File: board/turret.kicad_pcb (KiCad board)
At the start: 2 copper layers, 28 parts, among them Q1 2N3904, U1 W25Q32JVSS, U2 LM386

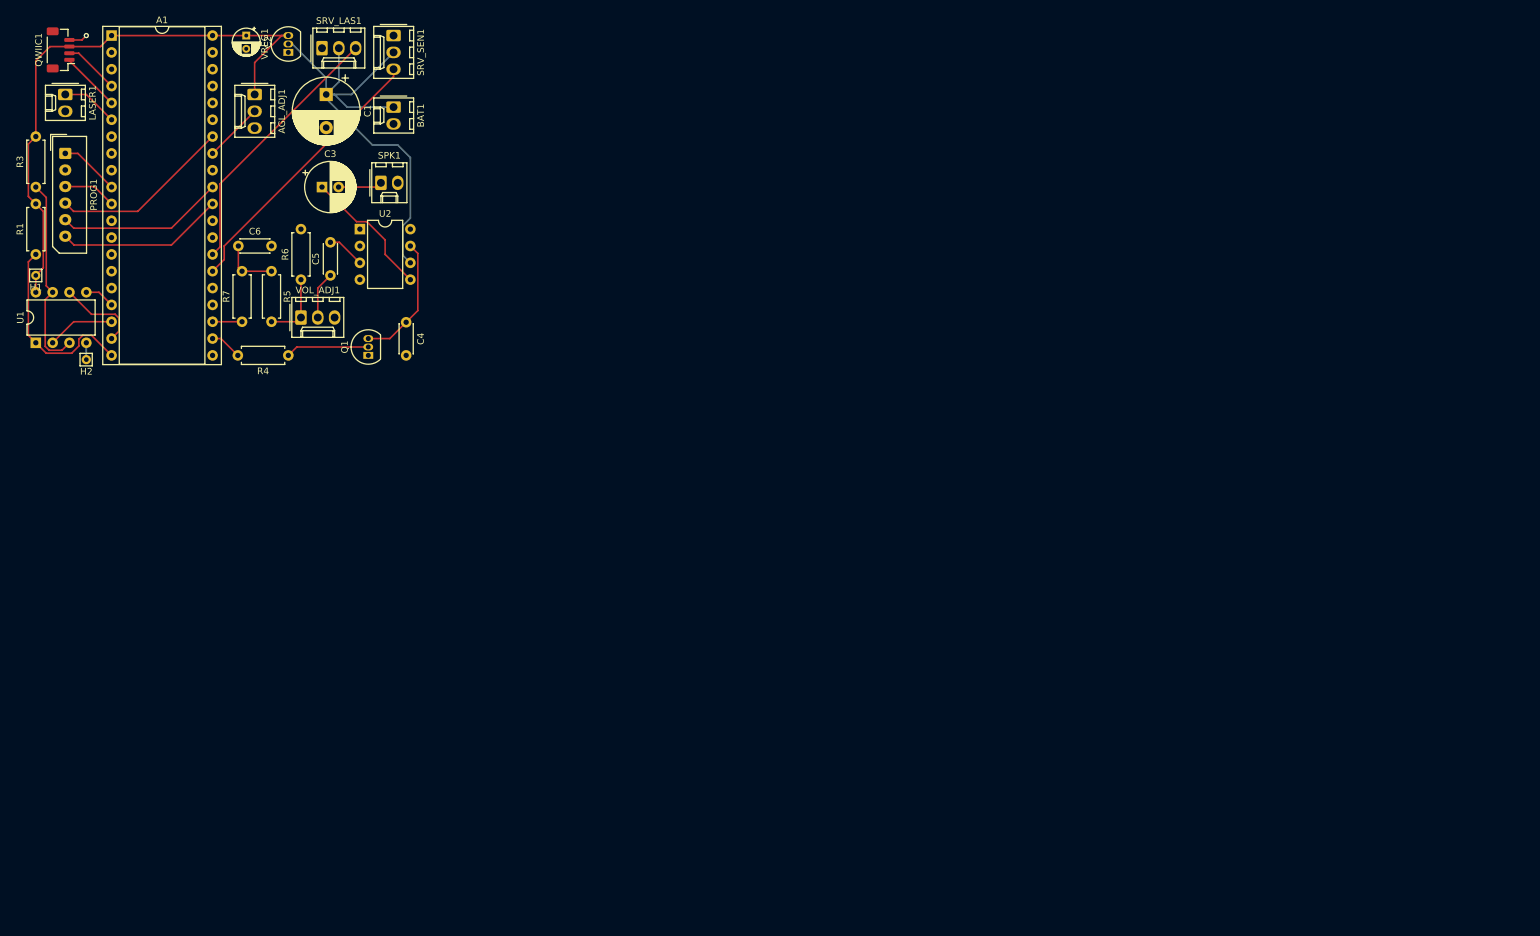
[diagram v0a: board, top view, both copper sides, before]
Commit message: Assign most components
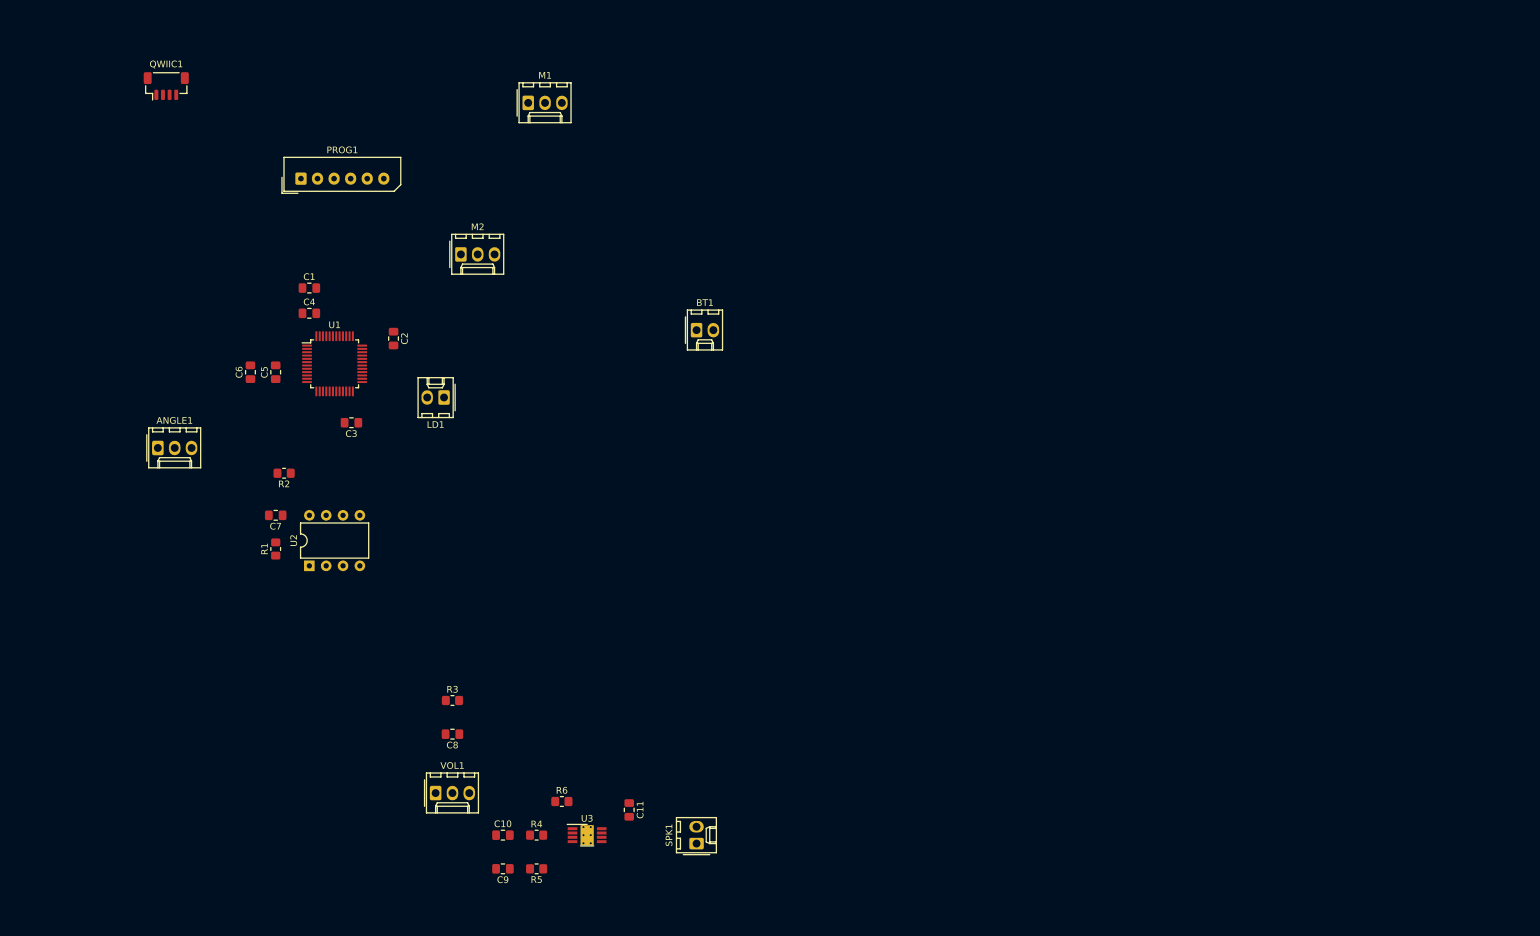
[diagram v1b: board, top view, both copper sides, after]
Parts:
- removed A1: Maple_Mini, Package_DIP:DIP-40_W15.24mm_Socket
- removed AGL_ADJ1: 10K, Connector_Molex:Molex_KK-254_AE-6410-03A_1x03_P2.54mm_Vertical
- removed BAT1: Battery, Connector_Molex:Molex_KK-254_AE-6410-02A_1x02_P2.54mm_Vertical
- removed H1: CAP_POS, Connector_Pin:Pin_D0.7mm_L6.5mm_W1.8mm_FlatFork
- removed H2: CAP_NEG, Connector_Pin:Pin_D0.7mm_L6.5mm_W1.8mm_FlatFork
- removed LASER1: Conn_01x02, Connector_Molex:Molex_KK-254_AE-6410-02A_1x02_P2.54mm_Vertical
- removed Q1: 2N3904, Package_TO_SOT_THT:TO-92_Inline
- removed R7: 560, Resistor_THT:R_Axial_DIN0207_L6.3mm_D2.5mm_P7.62mm_Horizontal
- removed SRV_LAS1, SRV_SEN1: Conn_01x03, Connector_Molex:Molex_KK-254_AE-6410-03A_1x03_P2.54mm_Vertical
- removed VOL_ADJ1: 2K, Connector_Molex:Molex_KK-254_AE-6410-03A_1x03_P2.54mm_Vertical
- removed VREG1: MCP1700-3302E_TO92, Package_TO_SOT_THT:TO-92_Inline
- added ANGLE1: 10K, Connector_Molex:Molex_KK-254_AE-6410-03A_1x03_P2.54mm_Vertical, F.Cu at (39.4, 77.5)
- added BT1: Battery, Connector_Molex:Molex_KK-254_AE-6410-02A_1x02_P2.54mm_Vertical, F.Cu at (120.7, 59.7)
- added C10: 10n, Capacitor_SMD:C_0805_2012Metric_Pad1.18x1.45mm_HandSolder, F.Cu at (91.4, 135.9)
- added C11: 100n, Capacitor_SMD:C_0805_2012Metric_Pad1.18x1.45mm_HandSolder, F.Cu at (110.5, 132.1)
- added C7: 100n, Capacitor_SMD:C_0805_2012Metric_Pad1.18x1.45mm_HandSolder, F.Cu at (57.1, 87.6)
- added C8: 100n, Capacitor_SMD:C_0805_2012Metric_Pad1.18x1.45mm_HandSolder, F.Cu at (83.8, 120.7)
- added C9: 10n, Capacitor_SMD:C_0805_2012Metric_Pad1.18x1.45mm_HandSolder, F.Cu at (91.4, 141.0)
- added LD1: Laserdiode_1C2A, Connector_Molex:Molex_KK-254_AE-6410-02A_1x02_P2.54mm_Vertical, F.Cu at (82.5, 69.8)
- added M1: SRV_LAS, Connector_Molex:Molex_KK-254_AE-6410-03A_1x03_P2.54mm_Vertical, F.Cu at (95.2, 25.4)
- added M2: SRV_SEN, Connector_Molex:Molex_KK-254_AE-6410-03A_1x03_P2.54mm_Vertical, F.Cu at (85.1, 48.3)
- added R2: 50K, Resistor_SMD:R_0805_2012Metric_Pad1.20x1.40mm_HandSolder, F.Cu at (58.4, 81.3)
- added U3: TPA2005D1DGN, Custom_IC:TI_VSSOP-PowerPAD-8_3.0x3.0mm_P0.65mm_ThermalVias, F.Cu at (104.1, 135.9)
- added VOL1: 10K, Connector_Molex:Molex_KK-254_AE-6410-03A_1x03_P2.54mm_Vertical, F.Cu at (81.3, 129.5)
- C1: value 1000uF -> 4u7; footprint Capacitor_THT:CP_Radial_D10.0mm_P5.00mm -> Capacitor_SMD:C_0805_2012Metric_Pad1.18x1.45mm_HandSolder
- C2: value 1uF -> 100n; footprint Capacitor_THT:CP_Radial_D4.0mm_P2.00mm -> Capacitor_SMD:C_0805_2012Metric_Pad1.18x1.45mm_HandSolder
- C3: value 220uF -> 100n; footprint Capacitor_THT:CP_Radial_D7.5mm_P2.50mm -> Capacitor_SMD:C_0805_2012Metric_Pad1.18x1.45mm_HandSolder
- C4: value 100 nF -> 100n; footprint Capacitor_THT:C_Disc_D4.3mm_W1.9mm_P5.00mm -> Capacitor_SMD:C_0805_2012Metric_Pad1.18x1.45mm_HandSolder
- C5: value 100 nF -> 1u; footprint Capacitor_THT:C_Disc_D4.3mm_W1.9mm_P5.00mm -> Capacitor_SMD:C_0805_2012Metric_Pad1.18x1.45mm_HandSolder
- C6: value 10 nF -> 10n; footprint Capacitor_THT:C_Disc_D4.3mm_W1.9mm_P5.00mm -> Capacitor_SMD:C_0805_2012Metric_Pad1.18x1.45mm_HandSolder
- R1: value 10K -> 50K; footprint Resistor_THT:R_Axial_DIN0207_L6.3mm_D2.5mm_P7.62mm_Horizontal -> Resistor_SMD:R_0805_2012Metric_Pad1.20x1.40mm_HandSolder
- R3: value 10K -> 400; footprint Resistor_THT:R_Axial_DIN0207_L6.3mm_D2.5mm_P7.62mm_Horizontal -> Resistor_SMD:R_0805_2012Metric_Pad1.20x1.40mm_HandSolder
- R4: value 1000K -> 150K; footprint Resistor_THT:R_Axial_DIN0207_L6.3mm_D2.5mm_P7.62mm_Horizontal -> Resistor_SMD:R_0805_2012Metric_Pad1.20x1.40mm_HandSolder
- R5: value 10K -> 150K; footprint Resistor_THT:R_Axial_DIN0207_L6.3mm_D2.5mm_P7.62mm_Horizontal -> Resistor_SMD:R_0805_2012Metric_Pad1.20x1.40mm_HandSolder
- R6: value 1K -> 50K; footprint Resistor_THT:R_Axial_DIN0207_L6.3mm_D2.5mm_P7.62mm_Horizontal -> Resistor_SMD:R_0805_2012Metric_Pad1.20x1.40mm_HandSolder
- SPK1: value Conn_01x02 -> Speaker
- U1: value W25Q32JVSS -> STM32F103CBTx; footprint Package_DIP:DIP-8_W7.62mm -> Package_QFP:LQFP-48_7x7mm_P0.5mm
- U2: value LM386 -> W25Q32JVSS
- moved SPK1 110.5 mm to (120.7, 137.2), turned to 90 degrees
- moved R3 99.8 mm to (83.8, 115.6), turned to 0 degrees
- moved R5 98.6 mm to (96.5, 141.0), turned to 180 degrees
- moved R6 88.0 mm to (100.3, 130.8), turned to 0 degrees
- moved R4 81.5 mm to (96.5, 135.9), turned to 0 degrees
- moved R1 57.3 mm to (57.1, 92.7)
- moved U2 51.4 mm to (62.2, 95.2), turned to 90 degrees
- moved C2 50.8 mm to (74.9, 61.0)
- moved U1 45.2 mm to (66.0, 64.8), turned to 0 degrees
- moved C3 35.8 mm to (68.6, 73.7), turned to 180 degrees
- moved PROG1 35.8 mm to (61.0, 36.8), turned to 0 degrees
- moved C1 29.3 mm to (62.2, 53.3), turned to 0 degrees
- moved C6 19.1 mm to (53.3, 66.0), turned to 90 degrees
- moved QWIIC1 16.9 mm to (40.6, 22.9), turned to 0 degrees
- moved C5 16.8 mm to (57.1, 66.0)
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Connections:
- C1 pad 1: +6V -> +3V3
- C1 pad 2: GND -> GNDA
- C2 pad 2: GND -> GNDA
- C3 pad 1: Net-(C3-Pad1) -> +3V3
- C3 pad 2: Net-(C3-Pad2) -> GNDA
- C4 pad 1: Net-(C4-Pad1) -> +3V3
- C4 pad 2: GND -> GNDA
- C5 pad 1: Net-(C5-Pad1) -> +3V3
- C5 pad 2: Net-(C5-Pad2) -> GNDA
- C6 pad 1: Net-(C6-Pad1) -> +3V3
- C6 pad 2: GND -> GNDA
- PROG1 pad 1: Net-(A1-Pad10) -> /SWCLK
- PROG1 pad 2: GND -> GNDA
- PROG1 pad 3: Net-(A1-Pad11) -> /SWDIO
- PROG1 pad 4: Net-(A1-Pad34) -> /RESET
- PROG1 pad 5: Net-(A1-Pad31) -> /SER_TX
- PROG1 pad 6: Net-(A1-Pad30) -> /SER_RX
- QWIIC1 pad 1: Net-(A1-Pad5) -> GNDA
- QWIIC1 pad 2: Net-(A1-Pad4) -> +3V3
- QWIIC1 pad 3: +3V3 -> /SDA
- QWIIC1 pad 4: GND -> /SCL
- R1 pad 1: Net-(A1-Pad20) -> /SPI_NSS
- R3 pad 1: Net-(R3-Pad1) -> /AUDIO
- R3 pad 2: +3V3 -> Net-(C8-Pad1)
- R4 pad 2: Mute -> Net-(R4-Pad2)
- R5 pad 1: Net-(C6-Pad1) -> Net-(R5-Pad1)
- R5 pad 2: Net-(R5-Pad2) -> Net-(C9-Pad1)
- R6 pad 1: Net-(R5-Pad2) -> /MUTE
- R6 pad 2: GND -> Net-(R6-Pad2)
- SPK1 pad 1: Net-(C3-Pad2) -> Net-(SPK1-Pad1)
- SPK1 pad 2: GND -> Net-(SPK1-Pad2)
- U1 pad 1: Net-(A1-Pad20) -> +3V3
- U1 pad 2: Net-(A1-Pad18) -> (no net)
- U1 pad 3: Net-(R3-Pad1) -> (no net)
- U1 pad 4: GND -> (no net)
- U1 pad 5: Net-(A1-Pad17) -> (no net)
- U1 pad 6: Net-(A1-Pad19) -> (no net)
- U1 pad 7: Net-(R3-Pad1) -> /RESET
- U1 pad 8: +3V3 -> GNDA
- U2 pad 1: Net-(U2-Pad1) -> /SPI_NSS
- U2 pad 2: GND -> /SPI_MISO
- U2 pad 3: Net-(C5-Pad2) -> Net-(R2-Pad1)
- U2 pad 4: GND -> GNDA
- U2 pad 5: Net-(C3-Pad1) -> /SPI_MOSI
- U2 pad 6: +6V -> /SPI_SCK
- U2 pad 7: Net-(C4-Pad1) -> Net-(R2-Pad1)
- U2 pad 8: Net-(U2-Pad8) -> +3V3
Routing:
- net +3V3: track 88.0 -> 0.00 mm
- net +6V: track 75.7 -> 0.00 mm
- net SRV_SEN: track 41.8 -> 0.00 mm
- net SRV_LAS: track 40.1 -> 0.00 mm
- net Net-(R3-Pad1): track 29.9 -> 0.00 mm
- net Net-(A1-Pad20): track 29.3 -> 0.00 mm
- net Net-(A1-Pad34): track 27.4 -> 0.00 mm
- net Net-(A1-Pad30): track 25.3 -> 0.00 mm
- net Net-(A1-Pad31): track 25.3 -> 0.00 mm
- net Net-(C3-Pad1): track 20.4 -> 0.00 mm
- net Net-(C4-Pad1): track 19.4 -> 0.00 mm
- net Net-(A1-Pad19): track 12.6 -> 0.00 mm
- net Net-(C10-Pad2): track 12.6 -> 0.00 mm
- net Net-(R5-Pad2): track 10.4 -> 0.00 mm
- net Net-(A1-Pad18): track 10.2 -> 0.00 mm
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
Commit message: Add PCB design
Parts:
- added C12: 22u, Capacitor_SMD:C_0603_1608Metric, F.Cu at (92.6, 67.3)
- added C13: 22u, Capacitor_SMD:C_0603_1608Metric, F.Cu at (92.6, 65.4)
- added C14: 4u7, Capacitor_SMD:C_0603_1608Metric, F.Cu at (91.4, 62.7)
- added C15: 100n, Capacitor_SMD:C_0603_1608Metric, F.Cu at (79.5, 52.1)
- added C16: 100n, Capacitor_SMD:C_0603_1608Metric, F.Cu at (79.5, 58.4)
- added C17: 1000u, Capacitor_THT:CP_Radial_D10.0mm_P5.00mm, F.Cu at (91.4, 56.5)
- added C18: 100p, Capacitor_SMD:C_0603_1608Metric, F.Cu at (91.9, 77.5)
- added C19: 20p, Capacitor_SMD:C_0603_1608Metric, F.Cu at (91.9, 79.4)
- added D1: LED, LED_SMD:LED_0805_2012Metric, F.Cu at (70.5, 56.6)
- added D2: D_Schottky, Diode_SMD:D_SMA, F.Cu at (90.1, 74.9)
- added L1: 2u2, Inductor_THT:L_Axial_L7.0mm_D3.3mm_P10.16mm_Horizontal_Fastron_MICC, F.Cu at (88.3, 71.8)
- added Q1: BC547, Package_TO_SOT_THT:TO-92_Inline_Wide, F.Cu at (97.2, 82.5)
- added R7: 5, Resistor_SMD:R_0603_1608Metric, F.Cu at (88.5, 77.5)
- added R8: 1K, Resistor_SMD:R_0603_1608Metric, F.Cu at (87.4, 82.5)
- added U4: TPS61322xADBV, Package_TO_SOT_SMD:SOT-23-5, F.Cu at (92.7, 70.5)
- added U5: TLV70028_SOT23-5, Package_TO_SOT_SMD:SOT-23-5, F.Cu at (79.4, 55.2)
- C1, C10, C11, C2, C3, C4, C5, C6, C8, C9: footprint Capacitor_SMD:C_0805_2012Metric_Pad1.18x1.45mm_HandSolder -> Capacitor_SMD:C_0603_1608Metric
- C7: footprint Capacitor_SMD:C_0805_2012Metric_Pad1.18x1.45mm_HandSolder -> Capacitor_SMD:C_0603_1608Metric; moved to B.Cu
- R1, R4, R5: footprint Resistor_SMD:R_0805_2012Metric_Pad1.20x1.40mm_HandSolder -> Resistor_SMD:R_0603_1608Metric
- R2: footprint Resistor_SMD:R_0805_2012Metric_Pad1.20x1.40mm_HandSolder -> Resistor_SMD:R_0603_1608Metric; moved to B.Cu
- R3: value 400 -> 200; footprint Resistor_SMD:R_0805_2012Metric_Pad1.20x1.40mm_HandSolder -> Resistor_SMD:R_0603_1608Metric
- R6: value 50K -> 50; footprint Resistor_SMD:R_0805_2012Metric_Pad1.20x1.40mm_HandSolder -> Resistor_SMD:R_0603_1608Metric
- moved R6 78.3 mm to (70.5, 58.4), turned to 180 degrees
- moved SPK1 68.3 mm to (78.7, 83.2)
- moved R5 66.0 mm to (64.6, 83.2)
- moved C9 65.1 mm to (61.4, 83.2)
- moved U3 63.9 mm to (69.8, 81.9)
- moved R4 63.8 mm to (64.6, 80.6)
- moved C10 62.9 mm to (61.4, 80.6)
- moved C11 62.0 mm to (74.3, 81.8)
- moved VOL1 55.9 mm to (52.1, 81.9)
- moved C8 51.1 mm to (65.4, 73.0), turned to 0 degrees
- moved R3 48.1 mm to (65.4, 71.1), turned to 180 degrees
- moved M1 47.5 mm to (102.2, 72.4), turned to 90 degrees
- moved QWIIC1 35.4 mm to (61.6, 51.4)
- moved C7 30.1 mm to (74.9, 63.4), turned to 90 degrees
- moved R1 26.1 mm to (71.1, 70.6), turned to 270 degrees
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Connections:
- ANGLE1 pad 3: +3V3 -> VDD
- BT1 pad 1: +3V3 -> Net-(BT1-Pad1)
- BT1 pad 2: (no net) -> GNDA
- C1 pad 1: +3V3 -> VDD
- C11 pad 2: +3V3 -> +5V
- C2 pad 1: +3V3 -> VDD
- C3 pad 1: +3V3 -> VDD
- C4 pad 1: +3V3 -> VDD
- C5 pad 1: +3V3 -> VDD
- C6 pad 1: +3V3 -> VDD
- C7 pad 1: +3V3 -> VDD
- LD1 pad 1: GNDA -> Net-(LD1-Pad1)
- LD1 pad 2: /LASER -> +5V
- M1 pad 2: +3V3 -> +5V
- M2 pad 2: +3V3 -> +5V
- QWIIC1 pad 2: +3V3 -> VDD
- R1 pad 2: +3V3 -> VDD
- R2 pad 2: +3V3 -> VDD
- R6 pad 1: /MUTE -> Net-(D1-Pad2)
- R6 pad 2: Net-(R6-Pad2) -> /TGT_LED
- U1 pad 1: +3V3 -> VDD
- U1 pad 10: (no net) -> Net-(U1-Pad10)
- U1 pad 14: /SPI_NSS -> /AU_ENAB
- U1 pad 15: /SPI_SCK -> /LASER
- U1 pad 16: /SPI_MISO -> Net-(U1-Pad16)
- U1 pad 17: /SPI_MOSI -> Net-(U1-Pad17)
- U1 pad 18: (no net) -> /AUDIO
- U1 pad 19: (no net) -> Net-(U1-Pad19)
- U1 pad 2: (no net) -> Net-(U1-Pad2)
- U1 pad 20: (no net) -> Net-(U1-Pad20)
- U1 pad 21: (no net) -> Net-(U1-Pad21)
- U1 pad 22: (no net) -> Net-(U1-Pad22)
- U1 pad 24: +3V3 -> VDD
- U1 pad 25: (no net) -> /SPI_NSS
- U1 pad 26: (no net) -> /SPI_SCK
- U1 pad 27: /LASER -> /SPI_MISO
- U1 pad 28: (no net) -> /SPI_MOSI
- U1 pad 29: /AUDIO -> /SRV_SEN
- U1 pad 3: (no net) -> Net-(U1-Pad3)
- U1 pad 30: /MUTE -> /SRV_LAS
- U1 pad 31: (no net) -> Net-(U1-Pad31)
- U1 pad 32: (no net) -> Net-(U1-Pad32)
- U1 pad 33: (no net) -> Net-(U1-Pad33)
- U1 pad 36: +3V3 -> VDD
- U1 pad 38: (no net) -> Net-(U1-Pad38)
- U1 pad 39: (no net) -> /TGT_LED
- U1 pad 4: (no net) -> Net-(U1-Pad4)
- U1 pad 40: /SRV_SEN -> Net-(U1-Pad40)
- U1 pad 41: /SRV_LAS -> Net-(U1-Pad41)
- U1 pad 44: (no net) -> Net-(U1-Pad44)
- U1 pad 45: (no net) -> Net-(U1-Pad45)
- U1 pad 46: (no net) -> Net-(U1-Pad46)
- U1 pad 48: +3V3 -> VDD
- U1 pad 5: (no net) -> Net-(U1-Pad5)
- U1 pad 6: (no net) -> Net-(U1-Pad6)
- U1 pad 9: +3V3 -> VDD
- U2 pad 8: +3V3 -> VDD
- U3 pad 1: Net-(R6-Pad2) -> /AU_ENAB
- U3 pad 2: (no net) -> Net-(U3-Pad2)
- U3 pad 6: +3V3 -> +5V
- U3 pad 9: (no net) -> GNDA
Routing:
- net GNDA: track 0.00 -> 103.0 mm, vias 0 -> 14
- net VDD: track 0.00 -> 89.2 mm, vias 0 -> 2
- net +5V: track 0.00 -> 78.8 mm, vias 0 -> 2
- net /SRV_LAS: track 0.00 -> 69.0 mm
- net /SRV_SEN: track 0.00 -> 58.6 mm
- net Net-(BT1-Pad1): track 0.00 -> 42.3 mm, vias 0 -> 3
- net /LASER: track 0.00 -> 32.6 mm
- net /SPI_SCK: track 0.00 -> 24.9 mm
- net /SWCLK: track 0.00 -> 23.4 mm, vias 0 -> 1
- net /SWDIO: track 0.00 -> 20.9 mm, vias 0 -> 1
- net Net-(C8-Pad1): track 0.00 -> 15.9 mm, vias 0 -> 2
- net /RESET: track 0.00 -> 15.5 mm, vias 0 -> 1
- net /SER_TX: track 0.00 -> 14.4 mm, vias 0 -> 1
- net /AU_ENAB: track 0.00 -> 14.2 mm
- net /SER_RX: track 0.00 -> 13.8 mm, vias 0 -> 1
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- added copper zone on B.Cu, net GNDA
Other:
- board outline added: 57.1 x 38.7 mm
- net class PWR added: clearance 0.2, trace_width 0.4, via_dia 0.8, via_drill 0.4

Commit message: Reroute 3v3 power
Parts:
- moved R1 2.62 mm to (71.8, 73.2), turned to 90 degrees
- moved C5 1.91 mm to (57.8, 65.9)
- moved C6 1.91 mm to (59.7, 65.9)
- moved R2 0.80 mm to (78.1, 63.5), turned to 90 degrees
- moved C7 0.12 mm to (74.9, 63.5)
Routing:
- net /SER_TX: track 14.4 -> 30.2 mm, vias 1 -> 0
- net /SER_RX: track 13.8 -> 27.9 mm, vias 1 -> 0
- net /SPI_NSS: track 8.73 -> 12.4 mm
- net /RESET: track 15.5 -> 12.3 mm, vias 1 -> 0
- net VDD: track 89.2 -> 92.2 mm, vias 2 -> 5

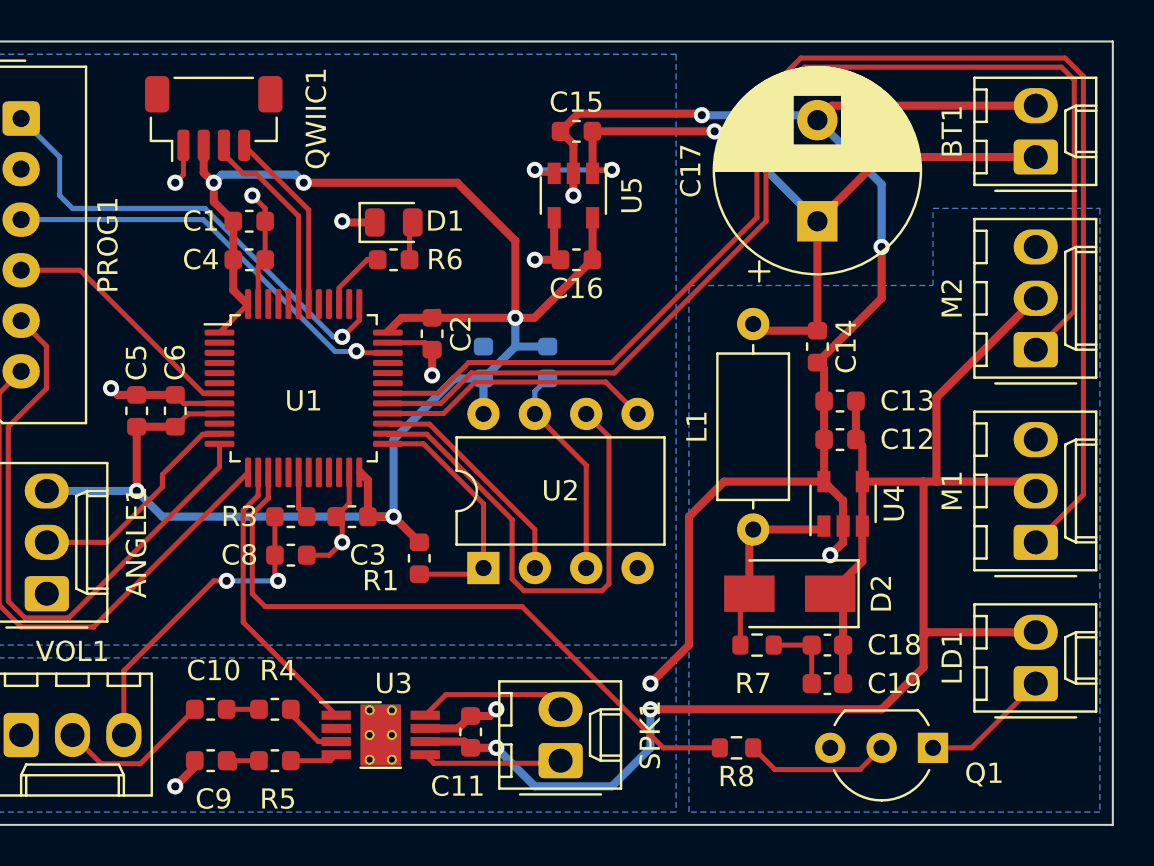
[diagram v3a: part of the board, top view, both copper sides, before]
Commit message: Add mounting holes
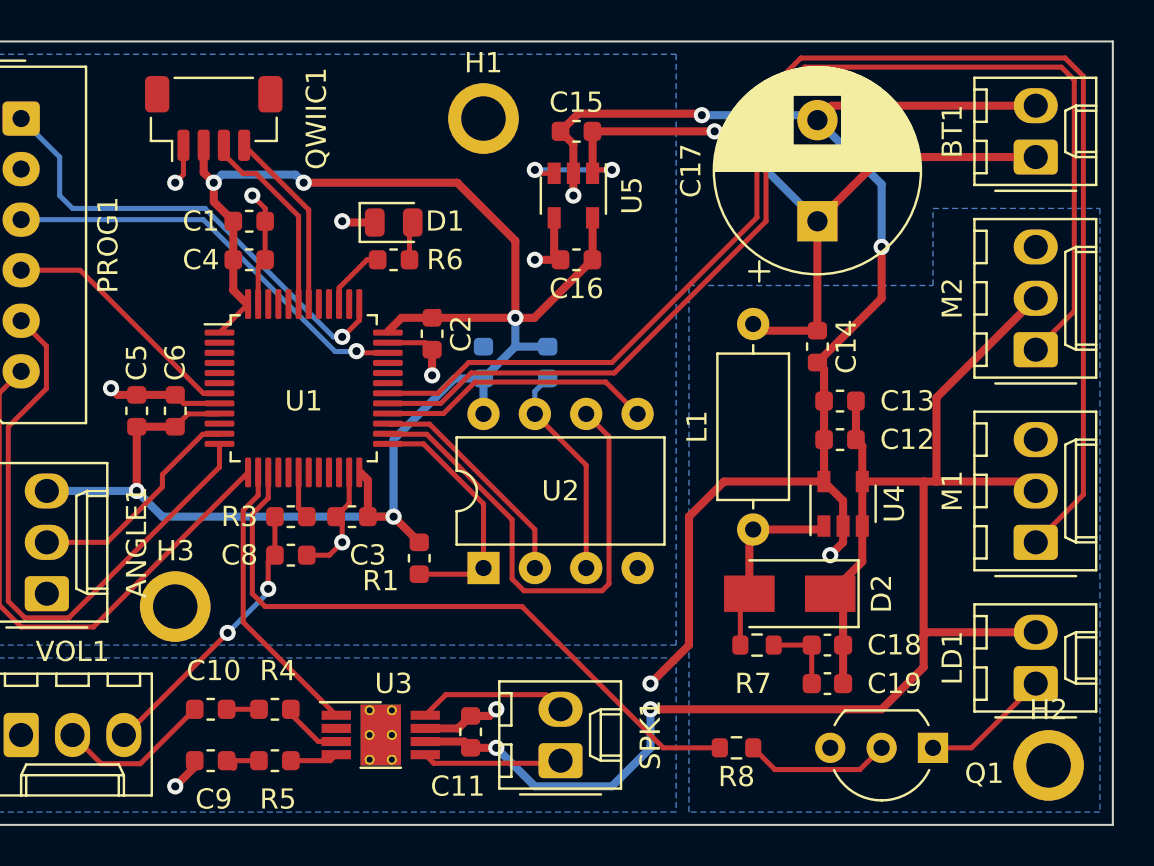
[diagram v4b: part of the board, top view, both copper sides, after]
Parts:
- added H1: MountingHole_Pad, MountingHole:MountingHole_2.2mm_M2_ISO7380_Pad, F.Cu at (74.9, 51.4)
- added H2: MountingHole_Pad, MountingHole:MountingHole_2.2mm_M2_ISO7380_Pad, F.Cu at (102.9, 83.4)
- added H3: MountingHole_Pad, MountingHole:MountingHole_2.2mm_M2_ISO7380_Pad, F.Cu at (59.7, 75.6)
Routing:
- net Net-(C8-Pad1): track 15.9 -> 13.9 mm
